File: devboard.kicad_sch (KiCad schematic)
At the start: 26 parts, among them J1 USB_C_Receptacle_USB2.0_14P, U1 RP2040, U2 NCP1117-3.3_SOT223, U3 W25Q128JVS, Y1 12 MHz

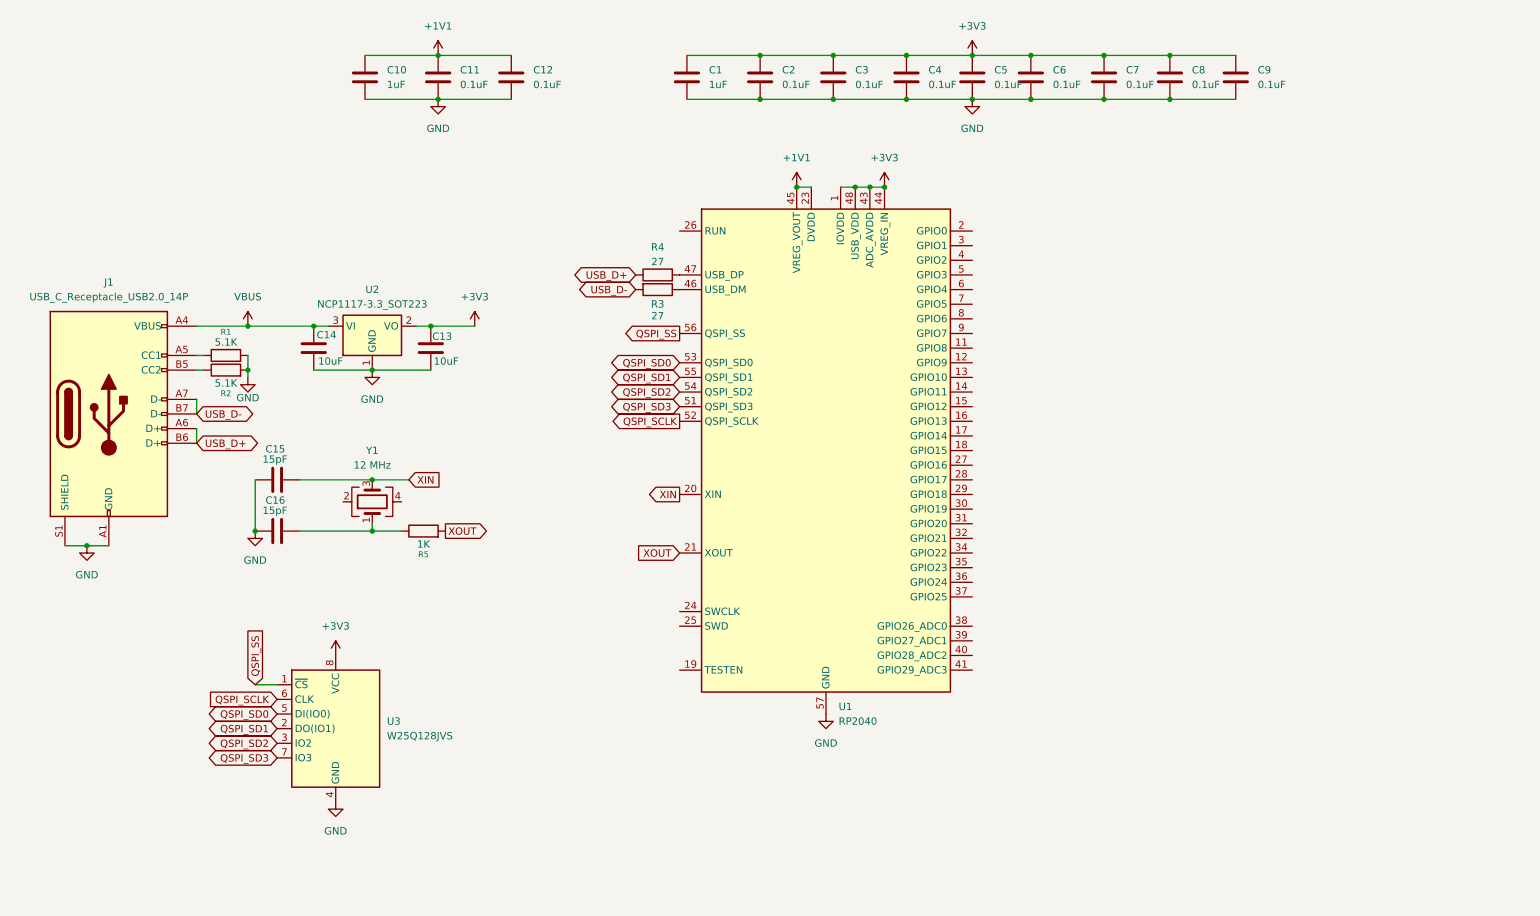
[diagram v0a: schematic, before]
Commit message: finished schematics...next is footprints :0
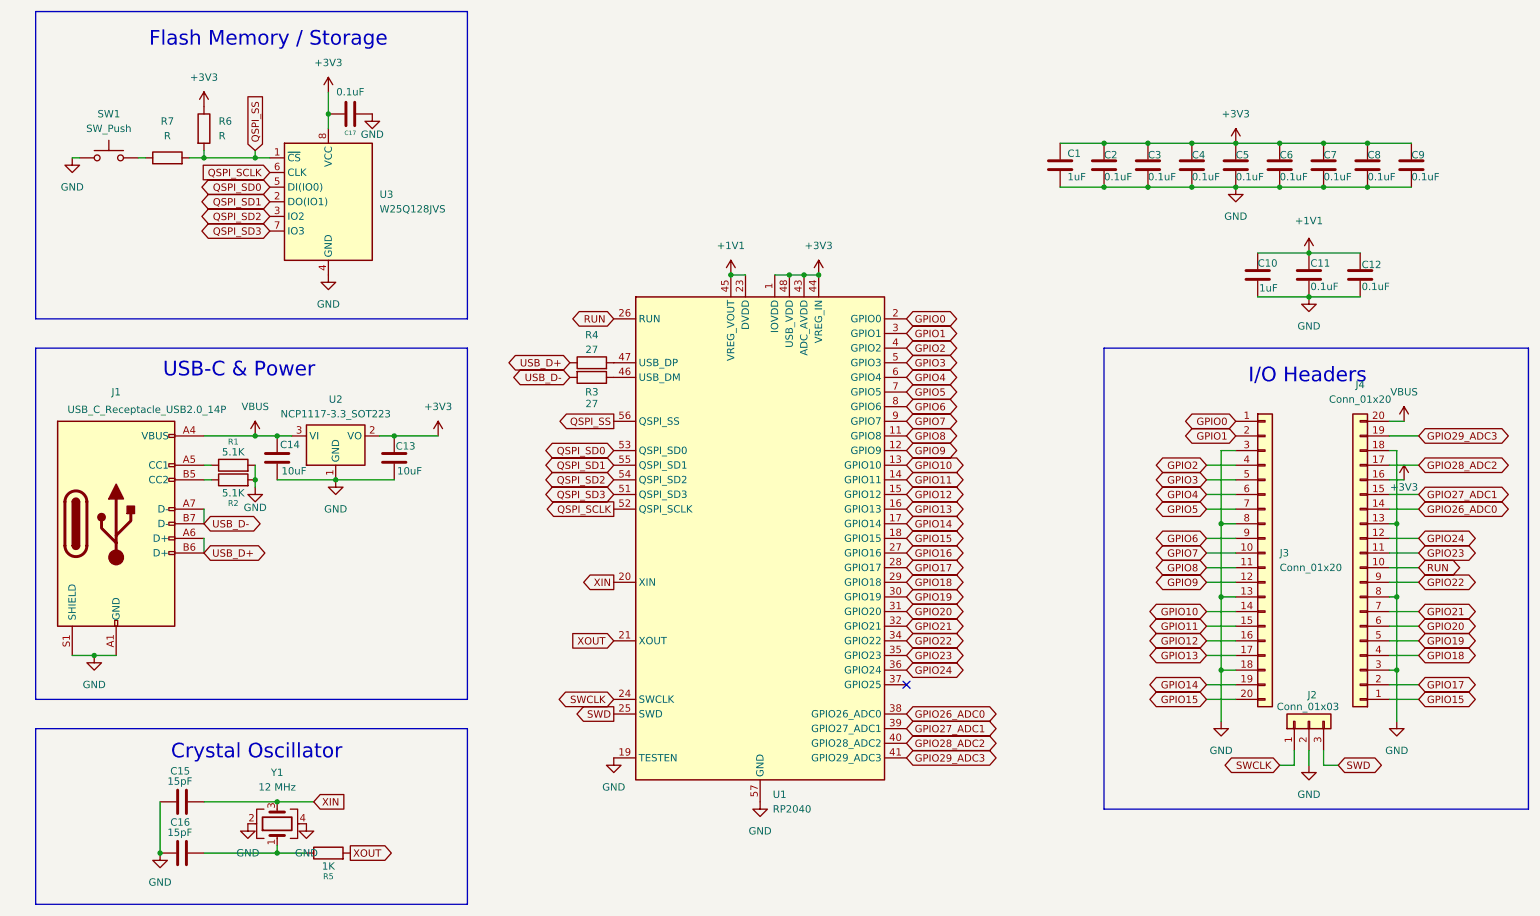
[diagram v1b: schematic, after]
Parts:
- added C17: 0.1uF, symbol Device:C
- added J2: Conn_01x03, symbol Connector_Generic:Conn_01x03
- added J3, J4: Conn_01x20, symbol Connector_Generic:Conn_01x20
- added R6, R7: R, symbol Device:R
- added SW1: SW_Push, symbol Switch:SW_Push
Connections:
- net +3V3: now also C17.2, J4.16 (Pin_16), R6.1
- net GND: now also U1.19 (TESTEN), Y1.2, Y1.4, C17.1, J2.2 (Pin_2), J3.13 (Pin_13), J3.18 (Pin_18), J3.3 (Pin_3), J3.8 (Pin_8), J4.13 (Pin_13), J4.18 (Pin_18), J4.3 (Pin_3), J4.8 (Pin_8), SW1.1
- net QSPI_SS: now also R6.2, R7.2
- net VBUS: now also J4.20 (Pin_20)
- net GPIO8: now reaches U1.11 (GPIO8)
- net GPIO8: now also J3.11 (Pin_11)
- net GPIO9: now reaches U1.12 (GPIO9)
- net GPIO9: now also J3.12 (Pin_12)
- net GPIO10: now reaches U1.13 (GPIO10)
- net GPIO10: now also J3.14 (Pin_14)
- net GPIO11: now reaches U1.14 (GPIO11)
- net GPIO11: now also J3.15 (Pin_15)
- net GPIO12: now reaches U1.15 (GPIO12)
- net GPIO12: now also J3.16 (Pin_16)
- net GPIO13: now reaches U1.16 (GPIO13)
- net GPIO13: now also J3.17 (Pin_17)
- net GPIO14: now reaches U1.17 (GPIO14)
- net GPIO14: now also J3.19 (Pin_19)
- net GPIO15: now reaches U1.18 (GPIO15)
- net GPIO15: now also J3.20 (Pin_20), J4.1 (Pin_1)
- net GPIO0: now reaches U1.2 (GPIO0)
- net GPIO0: now also J3.1 (Pin_1)
- net SWCLK: now reaches U1.24 (SWCLK)
- net SWCLK: now also J2.1 (Pin_1)
- net SWD: now reaches U1.25 (SWD)
- net SWD: now also J2.3 (Pin_3)
- net RUN: now reaches U1.26 (RUN)
- net RUN: now also J4.10 (Pin_10)
- net GPIO16: now reaches U1.27 (GPIO16)
- net GPIO17: now reaches U1.28 (GPIO17)
- net GPIO17: now also J4.2 (Pin_2)
- net GPIO18: now reaches U1.29 (GPIO18)
- net GPIO18: now also J4.4 (Pin_4)
- net GPIO1: now reaches U1.3 (GPIO1)
- net GPIO1: now also J3.2 (Pin_2)
- net GPIO19: now reaches U1.30 (GPIO19)
- net GPIO19: now also J4.5 (Pin_5)
- net GPIO20: now reaches U1.31 (GPIO20)
- net GPIO20: now also J4.6 (Pin_6)
- net GPIO21: now reaches U1.32 (GPIO21)
- net GPIO21: now also J4.7 (Pin_7)
- net GPIO22: now reaches U1.34 (GPIO22)
- net GPIO22: now also J4.9 (Pin_9)
- net GPIO23: now reaches U1.35 (GPIO23)
- net GPIO23: now also J4.11 (Pin_11)
- net GPIO24: now reaches U1.36 (GPIO24)
- net GPIO24: now also J4.12 (Pin_12)
- net GPIO26_ADC0: now reaches U1.38 (GPIO26_ADC0)
- net GPIO26_ADC0: now also J4.14 (Pin_14)
- net GPIO27_ADC1: now reaches U1.39 (GPIO27_ADC1)
- net GPIO27_ADC1: now also J4.15 (Pin_15)
- net GPIO2: now reaches U1.4 (GPIO2)
- net GPIO2: now also J3.4 (Pin_4)
- net GPIO28_ADC2: now reaches U1.40 (GPIO28_ADC2)
- net GPIO28_ADC2: now also J4.17 (Pin_17)
- net GPIO29_ADC3: now reaches U1.41 (GPIO29_ADC3)
- net GPIO29_ADC3: now also J4.19 (Pin_19)
- net GPIO3: now reaches U1.5 (GPIO3)
- net GPIO3: now also J3.5 (Pin_5)
- net GPIO4: now reaches U1.6 (GPIO4)
- net GPIO4: now also J3.6 (Pin_6)
- net GPIO5: now reaches U1.7 (GPIO5)
- net GPIO5: now also J3.7 (Pin_7)
- net GPIO6: now reaches U1.8 (GPIO6)
- net GPIO6: now also J3.9 (Pin_9)
- net GPIO7: now reaches U1.9 (GPIO7)
- net GPIO7: now also J3.10 (Pin_10)
- new net: R7.1, SW1.2
- no-connect marks 0 -> 1
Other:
- note added: "Crystal Oscillator"
- note added: "Flash Memory / Storage"
- note added: "I/O Headers"
- note added: "USB-C & Power"
- moved on the sheet: C1, C10, C11, C12, C13, C14, C15, C16, C2, C3, C4, C5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

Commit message: layout is my biggest opp </3
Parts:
- removed U2: NCP1117-3.3_SOT223, Package_TO_SOT_SMD:SOT-223-3_TabPin2, symbol Regulator_Linear:NCP1117-3.3_SOT223
- added U4: MCP1700x-330xxTT, Package_TO_SOT_SMD:SOT-23, symbol Regulator_Linear:MCP1700x-330xxTT
- C1, C10, C11, C12, C17, C2, C3, C4, C5, C6, C7, C8, C9: footprint (none) -> Capacitor_SMD:C_0402_1005Metric
- C13, C14: footprint (none) -> Capacitor_SMD:C_0603_1608Metric
- C15, C16: value 15pF -> 33pF; footprint (none) -> Capacitor_SMD:C_0402_1005Metric
- J1: footprint (none) -> Connector_USB:USB_C_Receptacle_HRO_TYPE-C-31-M-12
- J2: footprint (none) -> Connector_PinHeader_2.54mm:PinHeader_1x03_P2.54mm_Vertical
- J3, J4: footprint (none) -> Connector_PinHeader_2.54mm:PinHeader_1x20_P2.54mm_Vertical
- R1, R2, R3, R4, R5: footprint (none) -> Resistor_SMD:R_0402_1005Metric
- R6: value R -> 10K; footprint (none) -> Resistor_SMD:R_0402_1005Metric
- R7: value R -> 1K; footprint (none) -> Resistor_SMD:R_0402_1005Metric
- SW1: footprint (none) -> Button_Switch_SMD:SW_Push_SPST_NO_Alps_SKRK
- U3: value W25Q128JVS -> W25Q16JVZPIQ TR; footprint Package_SO:SOIC-8_5.23x5.23mm_P1.27mm -> Package_SON:Winbond_USON-8-1EP_3x2mm_P0.5mm_EP0.2x1.6mm
- Y1: footprint (none) -> Crystal:Crystal_SMD_3225-4Pin_3.2x2.5mm
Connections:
- net +3V3: now also U4.2 (VO)
- net GND: now also U4.1 (GND)
- net VBUS: now also U4.3 (VI)
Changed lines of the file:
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@@
 			)
 		)
-		(property "Footprint" ""
+		(property "Footprint" "Connector_PinHeader_2.54mm:PinHeader_1x20_P2.54mm_Vertical"
 			(at 231.14 119.38 0)
 			(effects
@@
 			)
 		)
-		(property "Footprint" ""
+		(property "Footprint" "Capacitor_SMD:C_0402_1005Metric"
 			(at 230.8352 74.93 0)
 			(effects
@@
 			)
 		)
-		(property "Footprint" ""
+		(property "Footprint" "Resistor_SMD:R_0402_1005Metric"
 			(at 52.07 108.458 90)
 			(effects
@@
 			)
 		)
-		(property "Footprint" ""
+		(property "Footprint" "Resistor_SMD:R_0402_1005Metric"
 			(at 52.07 105.918 90)
 			(effects
@@
 			)
 		)
-		(property "Footprint" ""
+		(property "Footprint" "Capacitor_SMD:C_0402_1005Metric"
 			(at 239.7252 74.93 0)
 			(effects
@@
 			)
 		)
-		(property "Footprint" ""
+		(property "Footprint" "Capacitor_SMD:C_0402_1005Metric"
 			(at 242.2652 55.88 0)
 			(effects
@@
 			)
 		)
-		(property "Footprint" ""
+		(property "Footprint" "Capacitor_SMD:C_0402_1005Metric"
 			(at 249.8852 55.88 0)
 			(effects
@@
 		(on_board yes)
 		(dnp no)
-		(fields_autoplaced yes)
 		(property "Reference" "#PWR025"
 			(at 54.61 172.72 0)
@@
 		)
 		(property "Value" "GND"
-			(at 54.61 171.45 0)
+			(at 52.578 166.624 0)
 			(effects
 				(font
@@
 			)
 		)
-		(property "Value" "W25Q128JVS"
+		(property "Value" "W25Q16JVZPIQ TR"
 			(at 77.47 59.6899 0)
 			(effects
@@
 			)
 		)
-		(property "Footprint" "Package_SO:SOIC-8_5.23x5.23mm_P1.27mm"
+		(property "Footprint" "Package_SON:Winbond_USON-8-1EP_3x2mm_P0.5mm_EP0.2x1.6mm"
 			(at 68.58 58.42 0)
 			(effects
@@
 			)
 		)
-		(property "Footprint" ""
+		(property "Footprint" "Capacitor_SMD:C_0603_1608Metric"
 			(at 60.6552 106.68 0)
 			(effects
@@
 			)
 		)
-		(property "Footprint" ""
+		(property "Footprint" "Capacitor_SMD:C_0402_1005Metric"
 			(at 257.5052 55.88 0)
 			(effects
@@
 	)
 	(symbol
+		(lib_id "Regulator_Linear:MCP1700x-330xxTT")
+		(at 69.85 99.06 0)
+		(unit 1)
+		(exclude_from_sim no)
+		(in_bom yes)
+		(on_board yes)
+		(dnp no)
+		(fields_autoplaced yes)
+		(property "Reference" "U4"
+			(at 69.85 92.71 0)
+			(effects
+				(font
+					(size 1.27 1.27)
+				)
+			)
+		)
+		(property "Value" "MCP1700x-330xxTT"
+			(at 69.85 95.25 0)
+			(effects
+				(font
+					(size 1.27 1.27)
+				)
+			)
+		)
+		(property "Footprint" "Package_TO_SOT_SMD:SOT-23"
+			(at 69.85 93.345 0)
+			(effects
+				(font
+					(size 1.27 1.27)
+				)
+				(hide yes)
+			)
+		)
+		(property "Datasheet" "http://ww1.microchip.com/downloads/en/DeviceDoc/20001826D.pdf"
+			(at 69.85 99.06 0)
+			(effects
+				(font
+					(size 1.27 1.27)
+				)
+				(hide yes)
+			)
+		)
+		(property "Description" "250mA Low Quiscent Current LDO, 3.3V output, SOT-23"
+			(at 69.85 99.06 0)
+			(effects
+				(font
+					(size 1.27 1.27)
+				)
+				(hide yes)
+			)
+		)
+		(pin "3"
+		)
+		(pin "1"
+		)
+		(pin "2"
+		)
+		(instances
+			(project ""
+				(path "/9b4be8cc-925e-42f0-8353-546f5b805e4e"
+					(reference "U4")
+					(unit 1)
+				)
+			)
+		)
+	)
+	(symbol
 		(lib_id "Device:C")
 		(at 218.44 52.07 0)
@@
 			)
 		)
-		(property "Footprint" ""
+		(property "Footprint" "Capacitor_SMD:C_0402_1005Metric"
 			(at 219.4052 55.88 0)
 			(effects
@@
 			)
 		)
-		(property "Value" "R"
+		(property "Value" "1K"
 			(at 40.64 46.99 90)
 			(effects
@@
 			)
 		)
-		(property "Footprint" ""
+		(property "Footprint" "Resistor_SMD:R_0402_1005Metric"
 			(at 40.64 52.578 90)
 			(effects
@@
 			)
 		)
-		(property "Footprint" ""
+		(property "Footprint" "Connector_PinHeader_2.54mm:PinHeader_1x03_P2.54mm_Vertical"
 			(at 238.76 148.59 0)
 			(effects
@@
 			)
 		)
-		(property "Value" "15pF"
+		(property "Value" "33pF"
 			(at 40.64 159.004 90)
 			(effects
@@
 			)
 		)
-		(property "Footprint" ""
+		(property "Footprint" "Capacitor_SMD:C_0402_1005Metric"
 			(at 39.37 163.5252 0)
 			(effects
@@
 			)
 		)
-		(property "Value" "R"
+		(property "Value" "10K"
 			(at 49.53 46.9899 0)
 			(effects
@@
 			)
 		)
-		(property "Footprint" ""
+		(property "Footprint" "Resistor_SMD:R_0402_1005Metric"
 			(at 45.212 45.72 90)
 			(effects
@@
 			)
 		)
-		(property "Footprint" ""
+		(property "Footprint" "Crystal:Crystal_SMD_3225-4Pin_3.2x2.5mm"
 			(at 59.69 166.37 0)
 			(effects
@@
 			)
 		)
-		(property "Footprint" ""
+		(property "Footprint" "Capacitor_SMD:C_0402_1005Metric"
 			(at 227.0252 55.88 0)
 			(effects
@@
 			)
 		)
-		(property "Footprint" ""
+		(property "Footprint" "Capacitor_SMD:C_0402_1005Metric"
 			(at 68.58 44.1452 0)
 			(effects
@@
 			)
 		)
-		(property "Footprint" ""
+		(property "Footprint" "Connector_USB:USB_C_Receptacle_HRO_TYPE-C-31-M-12"
 			(at 35.56 114.3 0)
 			(effects
@@
 			)
 		)
-		(property "Footprint" ""
+		(property "Footprint" "Capacitor_SMD:C_0402_1005Metric"
 			(at 204.1652 55.88 0)
 			(effects
@@
 		(on_board yes)
 		(dnp no)
-		(fields_autoplaced yes)
 		(property "Reference" "#PWR026"
 			(at 64.77 172.72 0)
@@
 		)
 		(property "Value" "GND"
-			(at 64.77 171.45 0)
+			(at 66.802 166.624 0)
 			(effects
 				(font
@@
 			)
 		)
-		(property "Footprint" ""
+		(property "Footprint" "Capacitor_SMD:C_0402_1005Metric"
 			(at 211.7852 55.88 0)
 			(effects
@@
 			)
 		)
-		(property "Value" "15pF"
+		(property "Value" "33pF"
 			(at 40.64 167.894 90)
 			(effects
@@
 			)
 		)
-		(property "Footprint" ""
+		(property "Footprint" "Capacitor_SMD:C_0402_1005Metric"
 			(at 39.37 172.4152 0)
 			(effects
@@
 			)
 		)
-		(property "Footprint" ""
+		(property "Footprint" "Capacitor_SMD:C_0603_1608Metric"
 			(at 80.9752 106.68 0)
 			(effects
@@
 			)
 		)
-		(property "Footprint" ""
+		(property "Footprint" "Resistor_SMD:R_0402_1005Metric"
 			(at 114.3 88.138 90)
 			(effects
@@
 			)
 		)
-		(property "Footprint" ""
+		(property "Footprint" "Resistor_SMD:R_0402_1005Metric"
 			(at 68.58 173.228 90)
 			(effects
@@
 			)
 		)
-		(property "Footprint" ""
+		(property "Footprint" "Button_Switch_SMD:SW_Push_SPST_NO_Alps_SKRK"
 			(at 30.48 45.72 0)
 			(effects
@@
 			)
 		)
-		(property "Footprint" ""
+		(property "Footprint" "Connector_PinHeader_2.54mm:PinHeader_1x20_P2.54mm_Vertical"
 			(at 247.65 121.92 0)
 			(effects
@@
 			)
 		)
-		(property "Footprint" ""
+		(property "Footprint" "Capacitor_SMD:C_0402_1005Metric"
 			(at 234.6452 55.88 0)
 			(effects
@@
 	)
 	(symbol
-		(lib_id "Regulator_Linear:NCP1117-3.3_SOT223")
-		(at 69.85 99.06 0)
-		(unit 1)
-		(exclude_from_sim no)
-		(in_bom yes)
-		(on_board yes)
-		(dnp no)
-		(fields_autoplaced yes)
-		(property "Reference" "U2"
-			(at 69.85 92.71 0)
-			(effects
-				(font
-					(size 1.27 1.27)
-				)
-			)
-		)
-		(property "Value" "NCP1117-3.3_SOT223"
-			(at 69.85 95.25 0)
-			(effects
-				(font
-					(size 1.27 1.27)
-				)
-			)
-		)
-		(property "Footprint" "Package_TO_SOT_SMD:SOT-223-3_TabPin2"
-			(at 69.85 93.98 0)
-			(effects
-				(font
-					(size 1.27 1.27)
-				)
-				(hide yes)
-			)
-		)
-		(property "Datasheet" "http://www.onsemi.com/pub_link/Collateral/NCP1117-D.PDF"
-			(at 72.39 105.41 0)
-			(effects
-				(font
-					(size 1.27 1.27)
-				)
-				(hide yes)
-			)
-		)
-		(property "Description" "1A Low drop-out regulator, Fixed Output 3.3V, SOT-223"
-			(at 69.85 99.06 0)
-			(effects
-				(font
-					(size 1.27 1.27)
-				)
-				(hide yes)
-			)
-		)
-		(pin "1"
-		)
-		(pin "3"
-		)
-		(pin "2"
-		)
-		(instances
-			(project ""
-				(path "/9b4be8cc-925e-42f0-8353-546f5b805e4e"
-					(reference "U2")
-					(unit 1)
-				)
-			)
-		)
-	)
-	(symbol
 		(lib_id "power:GND")
 		(at 118.11 154.94 0)
@@
 			)
 		)
-		(property "Footprint" ""
+		(property "Footprint" "Capacitor_SMD:C_0402_1005Metric"
 			(at 248.6152 74.93 0)
 			(effects
@@
 			)
 		)
-		(property "Footprint" ""
+		(property "Footprint" "Capacitor_SMD:C_0402_1005Metric"
 			(at 196.5452 55.88 0)
 			(effects
@@
 			)
 		)
-		(property "Footprint" ""
+		(property "Footprint" "Resistor_SMD:R_0402_1005Metric"
 			(at 114.3 87.122 90)
 			(effects
